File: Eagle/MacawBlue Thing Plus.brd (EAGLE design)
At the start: 22.9 x 58.4 mm, 134 parts, among them J2 CORTEX_DEBUG, J5 USB-C, J8 U.FL, U1 MCP73831, U2 3.3V, U3 NM180100, U4 CH340E_MSOP10, U5 3.3V, U6 DPX202700DT-4162A1, Y1 32.768kHz

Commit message: Added 4-layer board
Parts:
- removed U$66: (no value), buzzard_labels (10):MIC0
- R5, R6: device SparkFun-Resistors:0603@1 -> SparkFun-Resistors:0603
- moved TP4 3.31 mm to (3.71, 7.92)
- moved TP5 1.07 mm to (2.74, 8.94)
- moved J2 0.32 mm to (5.50, 36.6)
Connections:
- net ~D19/A0: now also U3.G8; no longer U3.G9
- net ~D20/A1: now also U3.G9; no longer U3.G8
- net ~D22/A3: now also U3.F8; no longer U3.C9
- net ~D23/A4: now also U3.E8; no longer U3.B9
- net ~D24/A5: now also U3.B9; no longer U3.F8
- net ~D5: now also U3.D2; no longer U3.E3
- net ~D6: now also U3.F2; no longer U3.D2
- net ~D7: now also U3.E3; no longer U3.F2
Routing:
- net ~D15/QWIIC_SCL: track 69.0 -> 39.6 mm, vias 0 -> 1
- net ~D12/MISO: track 29.5 -> 16.6 mm
- net !RESET: track 68.8 -> 59.1 mm
- net ~D18/LED: track 33.6 -> 26.0 mm, vias 3 -> 2
- net ~D3/A6: track 19.1 -> 12.4 mm
- net ~D24/A5: track 13.4 -> 18.7 mm
- net SWDCK: track 19.7 -> 14.7 mm
- net ~D7: track 11.8 -> 15.5 mm, vias 2 -> 1
- net 3.3V: track 89.4 -> 93.1 mm, vias 6 -> 10
- net ~D9/A7: track 25.4 -> 21.7 mm, vias 2 -> 1
- net LORA_EN: track 21.6 -> 24.9 mm
- net ~D21/A2: track 26.9 -> 23.6 mm
- net RXI-0: track 23.2 -> 25.3 mm
- net ~D20/A1: track 20.9 -> 22.6 mm
- net ~D6: track 11.9 -> 10.2 mm
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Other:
- board text added: "Daniel Dobre"
- board text removed: "Alex Wende"

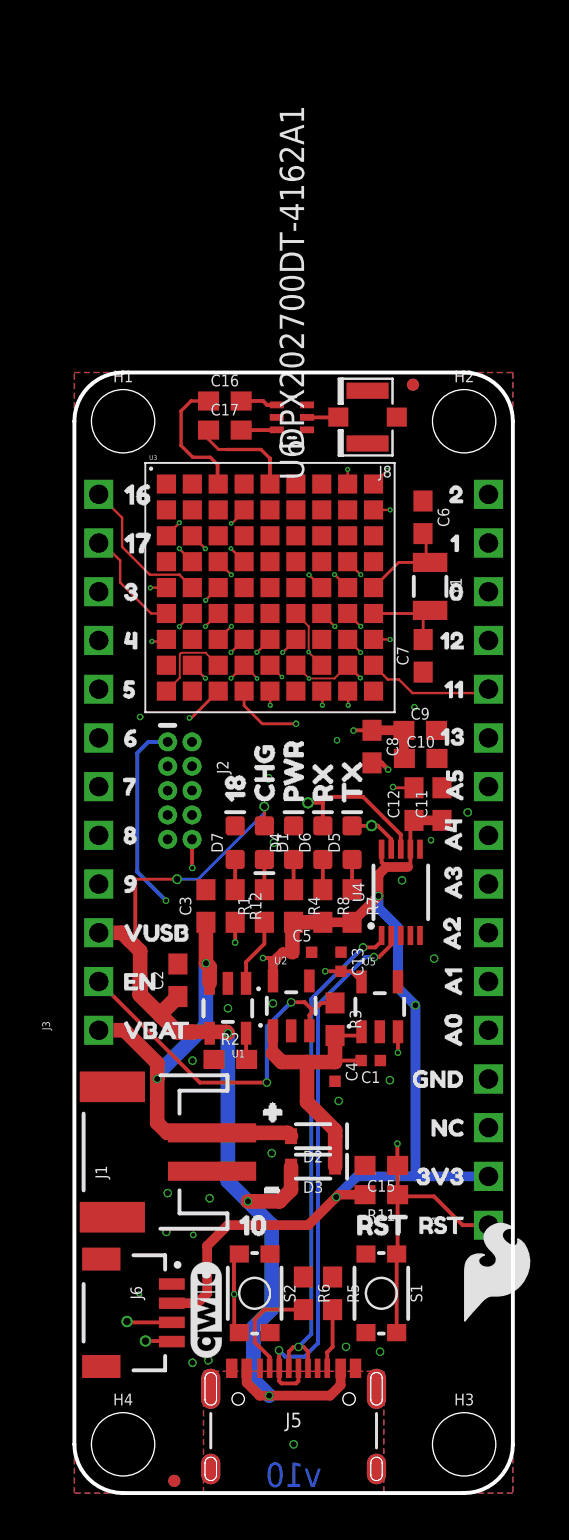
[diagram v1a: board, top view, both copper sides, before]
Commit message: Fixed NM180100 footprint
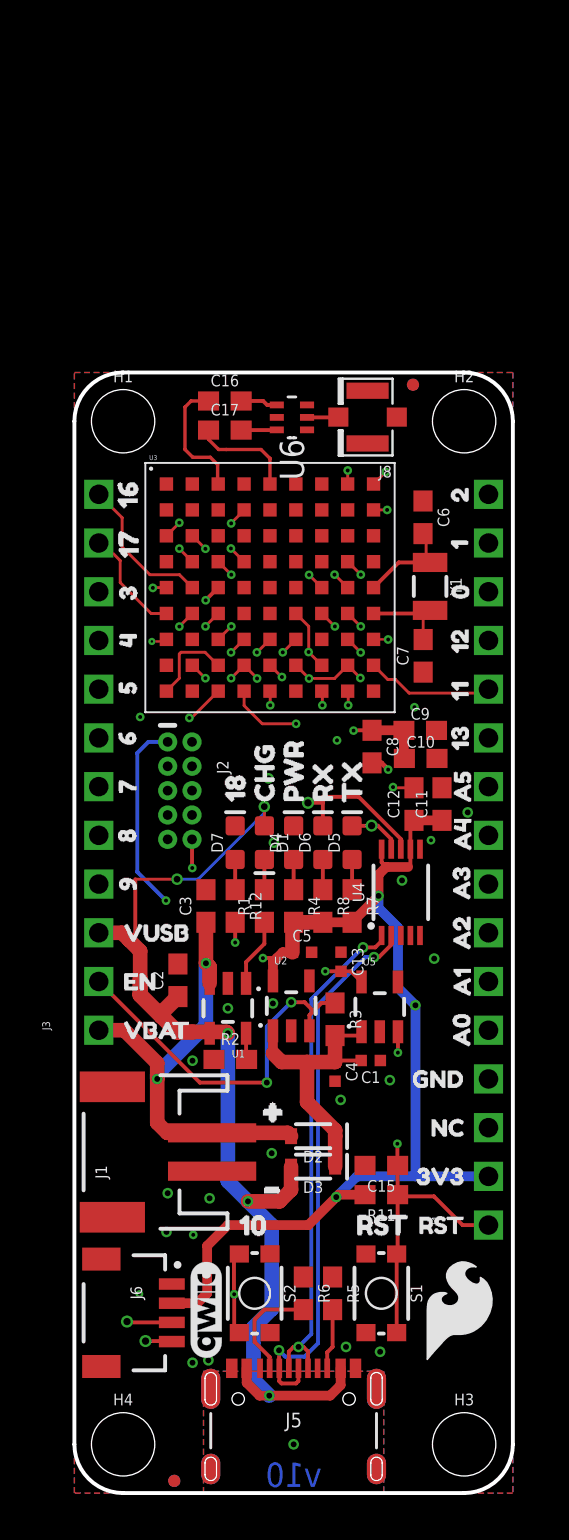
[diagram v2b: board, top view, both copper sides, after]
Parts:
- removed U$64: (no value), buzzard_labels (5):ARTEMIS_THING_PLUS0
- moved U$65 2.80 mm to (18.0, 6.69)
- moved U$17 2.58 mm to (20.1, 42.8), turned to 90 degrees
- moved U$18 2.36 mm to (20.1, 37.9), turned to 90 degrees
- moved U$16 2.14 mm to (20.1, 40.5), turned to 90 degrees
- moved U$2 2.00 mm to (2.82, 47.9), turned to 90 degrees
- moved U$1 1.93 mm to (2.77, 50.5), turned to 90 degrees
- moved U$15 1.82 mm to (20.1, 45.8), turned to 90 degrees
- moved U$13 1.82 mm to (20.1, 50.9), turned to 90 degrees
- moved U$8 1.76 mm to (2.74, 33.0), turned to 90 degrees
- moved U$7 1.74 mm to (2.77, 35.5), turned to 90 degrees
- moved U$14 1.69 mm to (20.1, 48.4), turned to 90 degrees
- moved U$3 1.61 mm to (2.79, 45.7), turned to 90 degrees
- moved U$4 1.55 mm to (2.79, 43.3), turned to 90 degrees
- moved U$9 1.53 mm to (2.79, 30.6), turned to 90 degrees
- moved U$6 1.52 mm to (2.74, 38.2), turned to 90 degrees
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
